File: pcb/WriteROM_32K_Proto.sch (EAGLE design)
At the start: 18 parts, among them IC1 23256-RP, IC2 XC9572XLTQG100, IC5 SST39SF040APHR

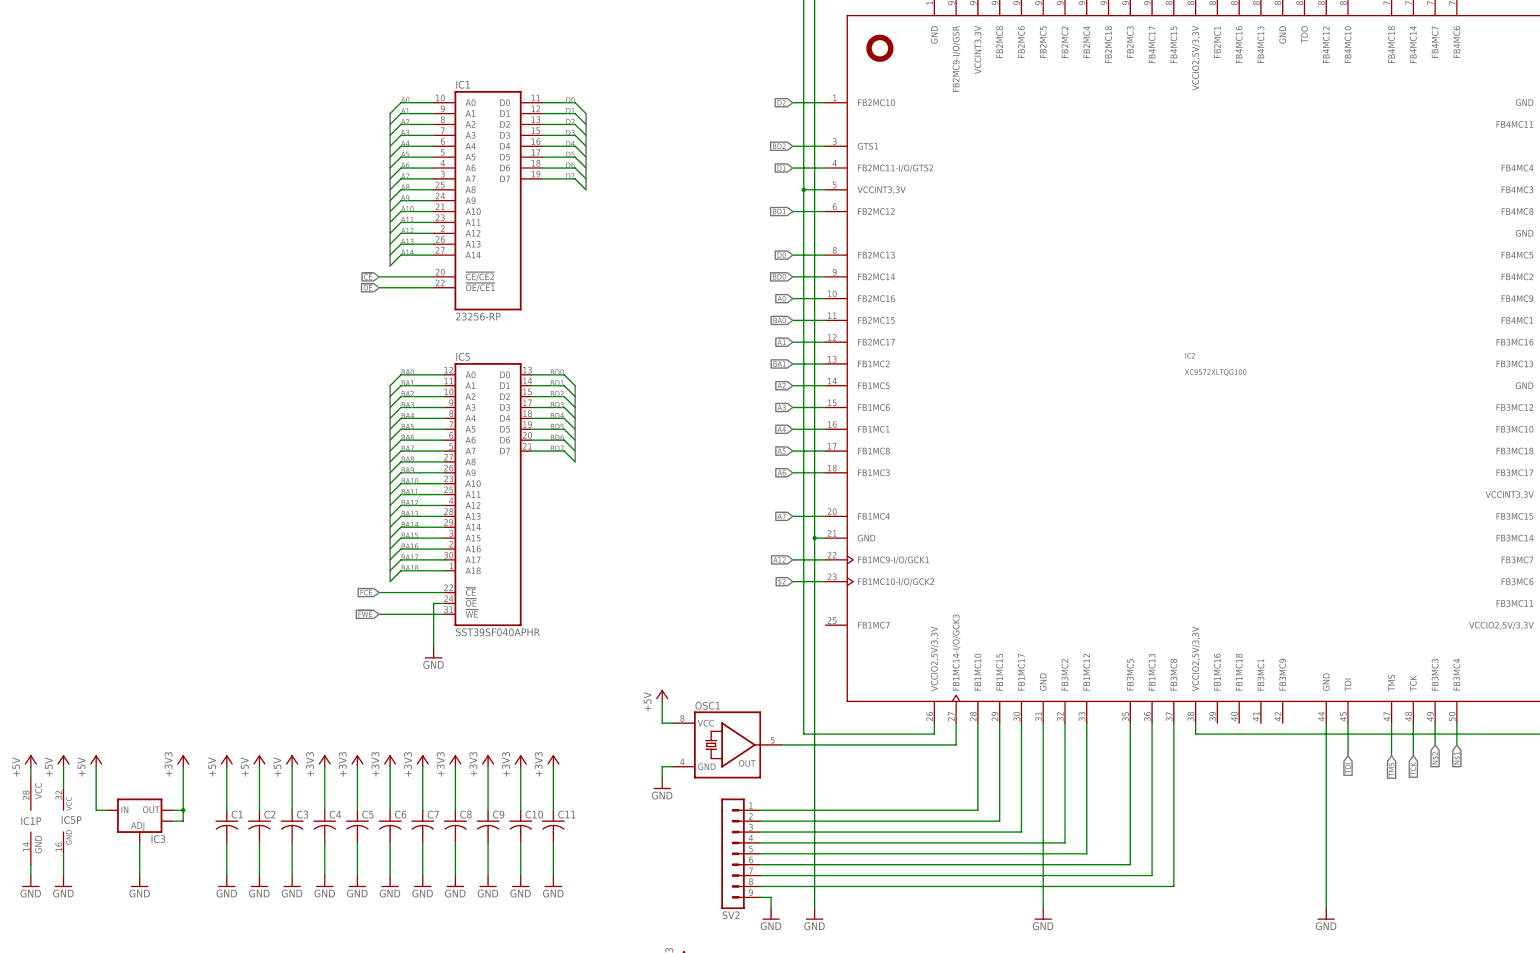
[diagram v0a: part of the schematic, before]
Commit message: Added more flexibility to banking
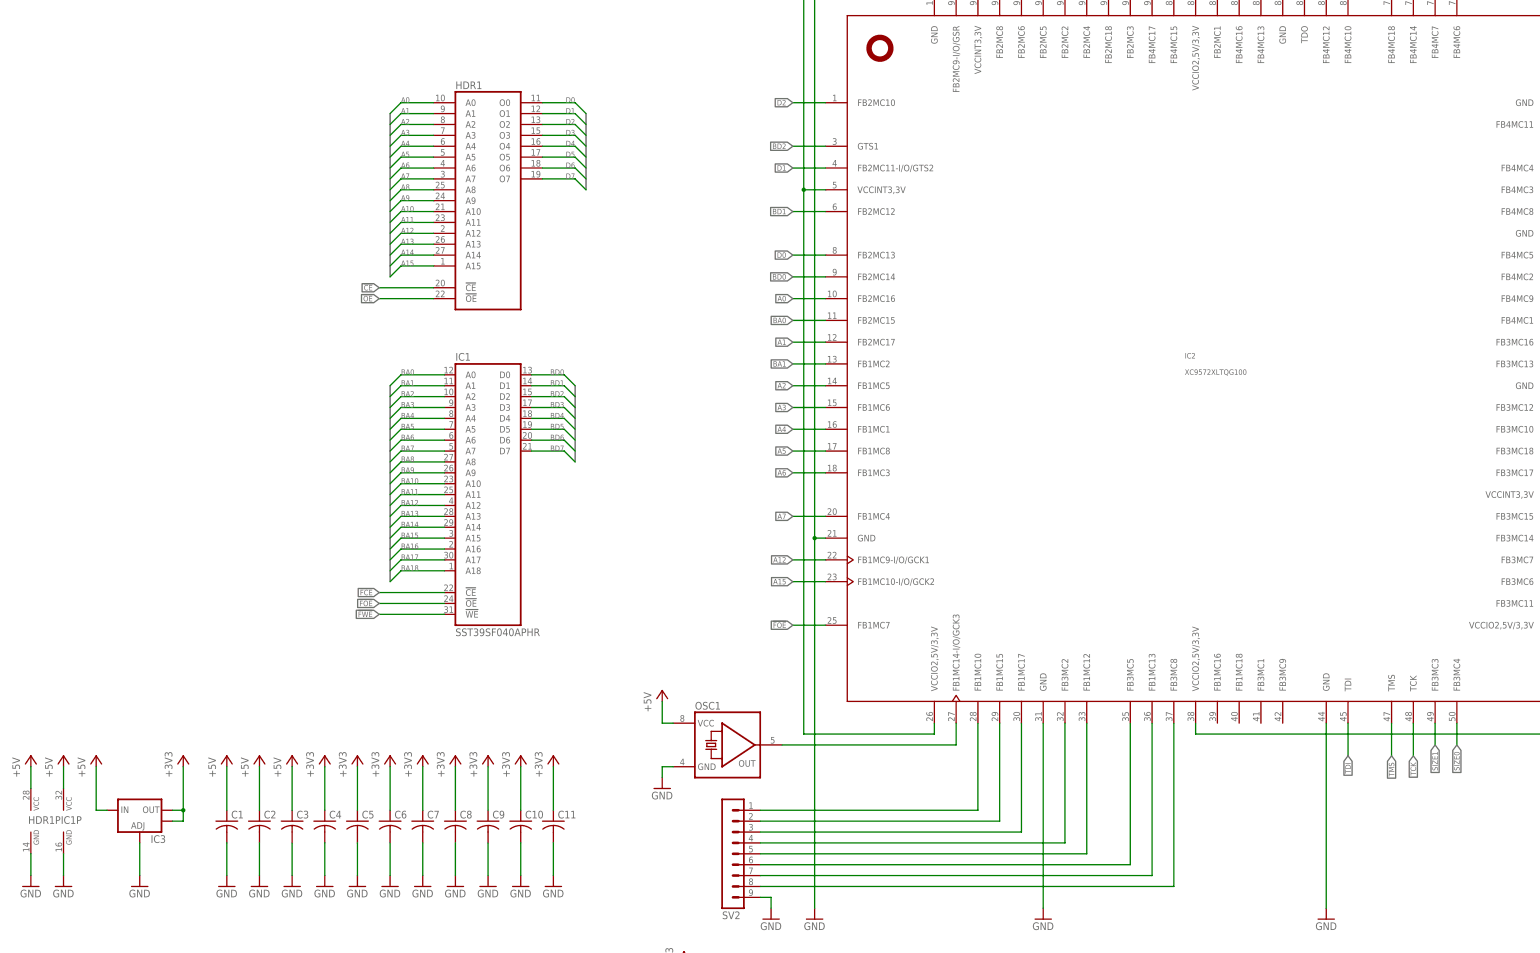
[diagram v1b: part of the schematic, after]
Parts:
- removed IC5: SST39SF040APHR, memory-sst:SST39SF040APHR
- added HDR1: (no value), memory-rp:27512
- IC1: value 23256-RP -> SST39SF040APHR; device commodore:23256-RP -> memory-sst:SST39SF040APHR
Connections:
- net N$1 renamed SIZE0
- net N$2 renamed SIZE1
- removed net $2: IC2.FB1MC10-I/O/GCK2
- new net !FOE: IC1A.!OE, IC2.FB1MC7
- new net A15: HDR1A.A15, IC2.FB1MC10-I/O/GCK2
- net !CE: now also HDR1A.!CE; no longer IC1A.!CE/CE2
- net !FCE: now also IC1A.!CE; no longer IC5A.!CE
- net !FWE: now also IC1A.!WE; no longer IC5A.!WE
- net !OE: now also HDR1A.!OE; no longer IC1A.!OE/CE1
- net +5V: now also HDR1P.VCC; no longer IC5P.VCC
- net A0: now also HDR1A.A0; no longer IC1A.A0
- net A1: now also HDR1A.A1; no longer IC1A.A1
- net A10: now also HDR1A.A10; no longer IC1A.A10
- net A11: now also HDR1A.A11; no longer IC1A.A11
- net A12: now also HDR1A.A12; no longer IC1A.A12
- net A13: now also HDR1A.A13; no longer IC1A.A13
- net A14: now also HDR1A.A14; no longer IC1A.A14
- net A2: now also HDR1A.A2; no longer IC1A.A2
- net A3: now also HDR1A.A3; no longer IC1A.A3
- net A4: now also HDR1A.A4; no longer IC1A.A4
- net A5: now also HDR1A.A5; no longer IC1A.A5
- net A6: now also HDR1A.A6; no longer IC1A.A6
- net A7: now also HDR1A.A7; no longer IC1A.A7
- net A8: now also HDR1A.A8; no longer IC1A.A8
- net A9: now also HDR1A.A9; no longer IC1A.A9
- net BA0: now also IC1A.A0; no longer IC5A.A0
- net BA1: now also IC1A.A1; no longer IC5A.A1
- net BA10: now also IC1A.A10; no longer IC5A.A10
- net BA11: now also IC1A.A11; no longer IC5A.A11
- net BA12: now also IC1A.A12; no longer IC5A.A12
- net BA13: now also IC1A.A13; no longer IC5A.A13
- net BA14: now also IC1A.A14; no longer IC5A.A14
- net BA15: now also IC1A.A15; no longer IC5A.A15
- net BA16: now also IC1A.A16; no longer IC5A.A16
- net BA17: now also IC1A.A17; no longer IC5A.A17
- net BA18: now also IC1A.A18; no longer IC5A.A18
- net BA2: now also IC1A.A2; no longer IC5A.A2
- net BA3: now also IC1A.A3; no longer IC5A.A3
- net BA4: now also IC1A.A4; no longer IC5A.A4
- net BA5: now also IC1A.A5; no longer IC5A.A5
- net BA6: now also IC1A.A6; no longer IC5A.A6
- net BA7: now also IC1A.A7; no longer IC5A.A7
- net BA8: now also IC1A.A8; no longer IC5A.A8
- net BA9: now also IC1A.A9; no longer IC5A.A9
- net BD0: now also IC1A.D0; no longer IC5A.D0
- net BD1: now also IC1A.D1; no longer IC5A.D1
- net BD2: now also IC1A.D2; no longer IC5A.D2
- net BD3: now also IC1A.D3; no longer IC5A.D3
- net BD4: now also IC1A.D4; no longer IC5A.D4
- net BD5: now also IC1A.D5; no longer IC5A.D5
- net BD6: now also IC1A.D6; no longer IC5A.D6
- net BD7: now also IC1A.D7; no longer IC5A.D7
- net D0: now also HDR1A.O0; no longer IC1A.D0
- net D1: now also HDR1A.O1; no longer IC1A.D1
- net D2: now also HDR1A.O2; no longer IC1A.D2
- net D3: now also HDR1A.O3; no longer IC1A.D3
- net D4: now also HDR1A.O4; no longer IC1A.D4
- net D5: now also HDR1A.O5; no longer IC1A.D5
- net D6: now also HDR1A.O6; no longer IC1A.D6
- net D7: now also HDR1A.O7; no longer IC1A.D7
- net GND: now also HDR1P.GND; no longer IC5A.!OE, IC5P.GND
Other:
- moved on the sheet: IC1P
